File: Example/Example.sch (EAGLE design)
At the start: 26 parts, among them IC2 74LS02D, U1 CD4017

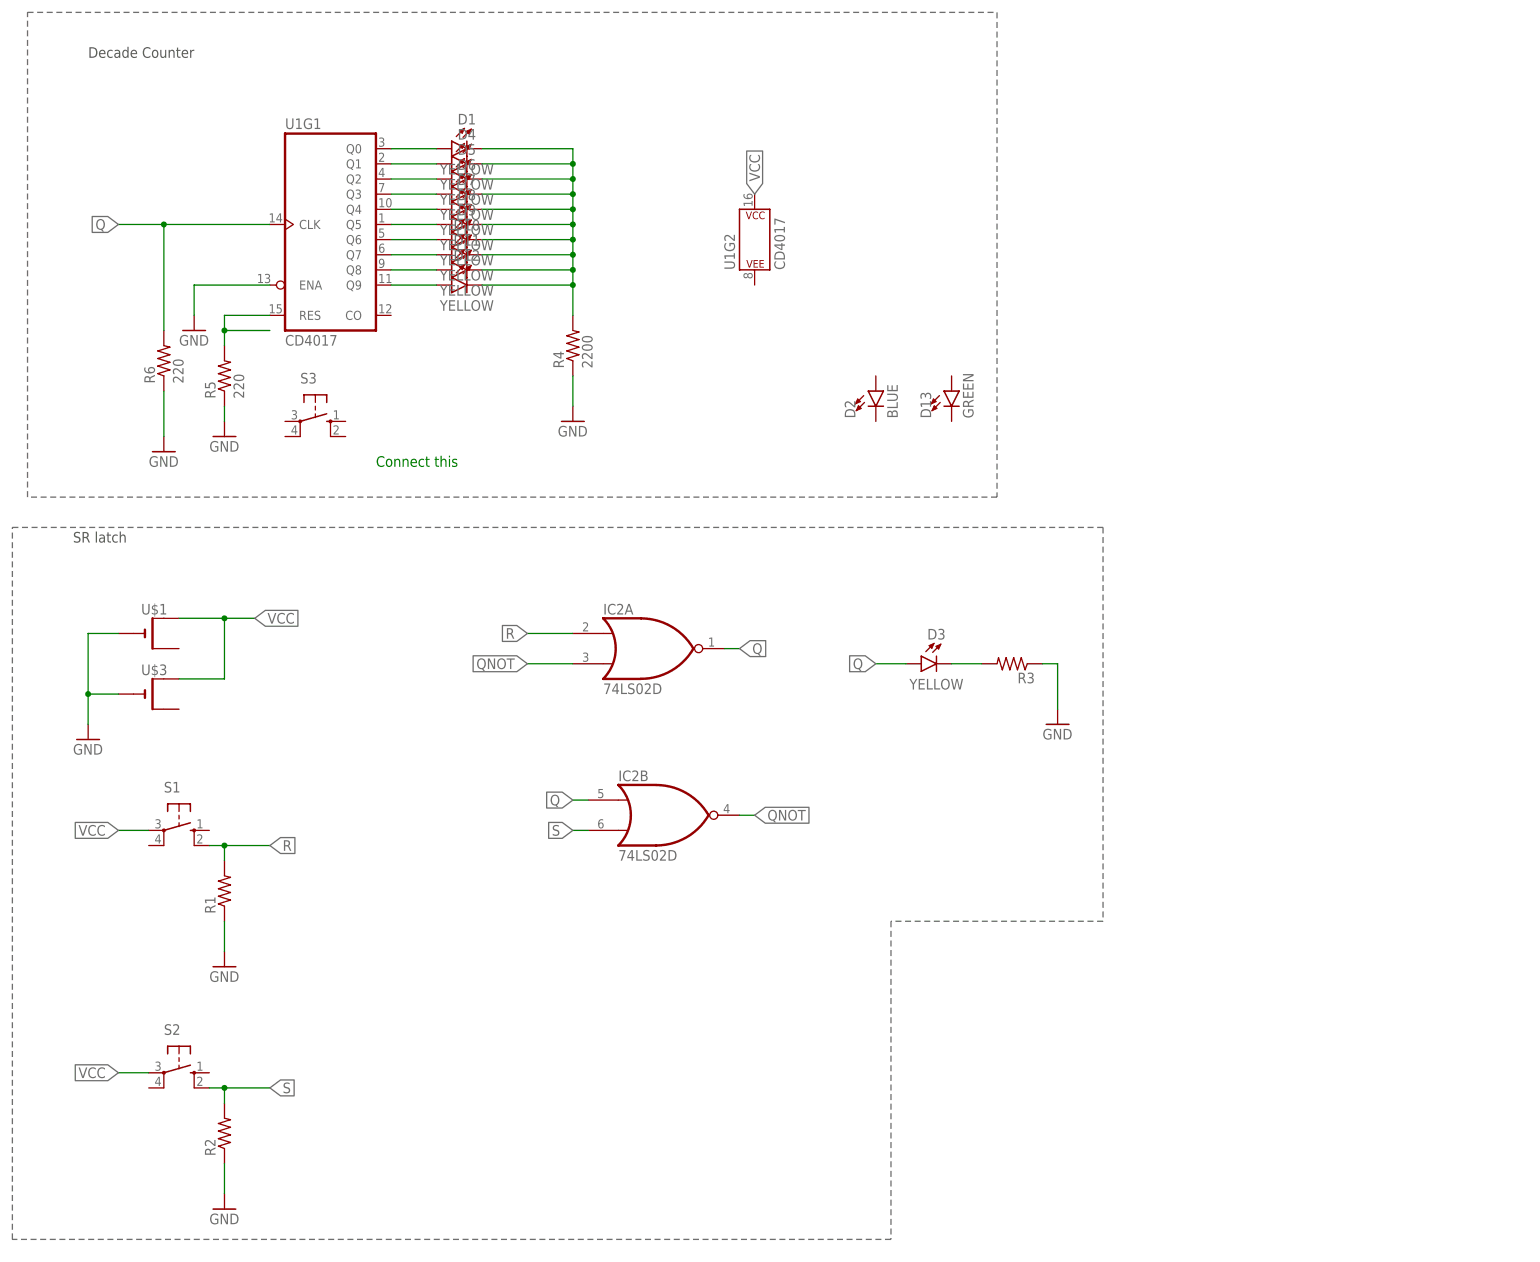
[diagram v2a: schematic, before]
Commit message: connected the reset button and change the titles for sheet
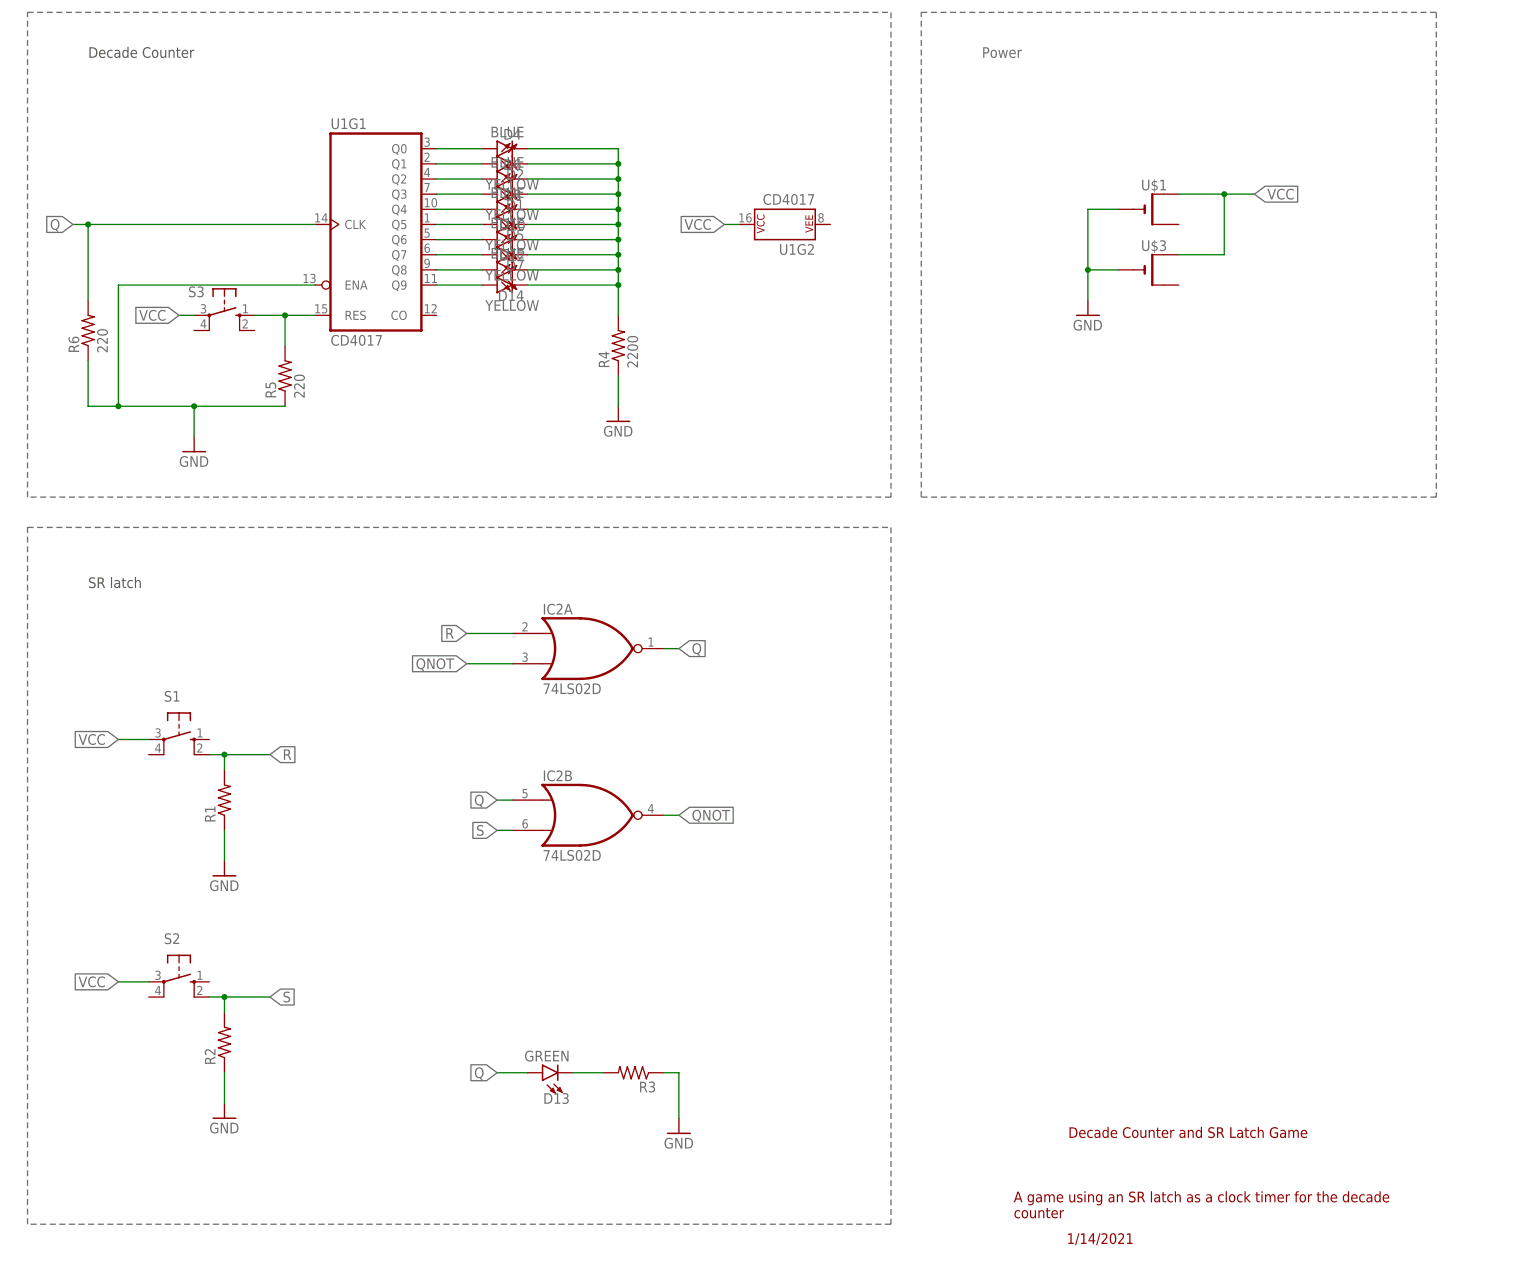
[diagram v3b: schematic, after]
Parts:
- removed D11, D3, D9: YELLOW, RoboJackets-LEDs:LED-SMD-YELLOW
- added D14: BLUE, RoboJackets-LEDs:LED-BLUE0603
- D1, D5, D7: value YELLOW -> BLUE; device RoboJackets-LEDs:LED-SMD-YELLOW -> RoboJackets-LEDs:LED-BLUE0603
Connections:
- removed net N$21: R5.2, U1G1.RES
- new net N$1: S3.P
- new net N$3: R5.2, S3.S, U1G1.RES
- net N$10: now also D2.A; no longer D1.A
- net N$12: now also D1.A; no longer D5.A
- net N$14: now also D5.A; no longer D7.A
- net N$16: now also D7.A; no longer D9.A
- net N$18: now also D14.A; no longer D11.A
- net N$2: now also D13.A; no longer D3.A
- net N$20: now also D14.C, D2.C; no longer D11.C, D9.C
- net N$5: now also D13.C; no longer D3.C
- net VCC: now also U1G2.P$V+
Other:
- note added: "1/14/2021"
- note added: "A game using an SR latch as a clock timer for the decade counter"
- note added: "Decade Counter and SR Latch Game"
- note added: "Power"
- note removed: "Connect this"
- moved on the sheet: D10, D12, D13, D2, D4, D6, D8, IC2A, IC2B, R1, R2, R3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

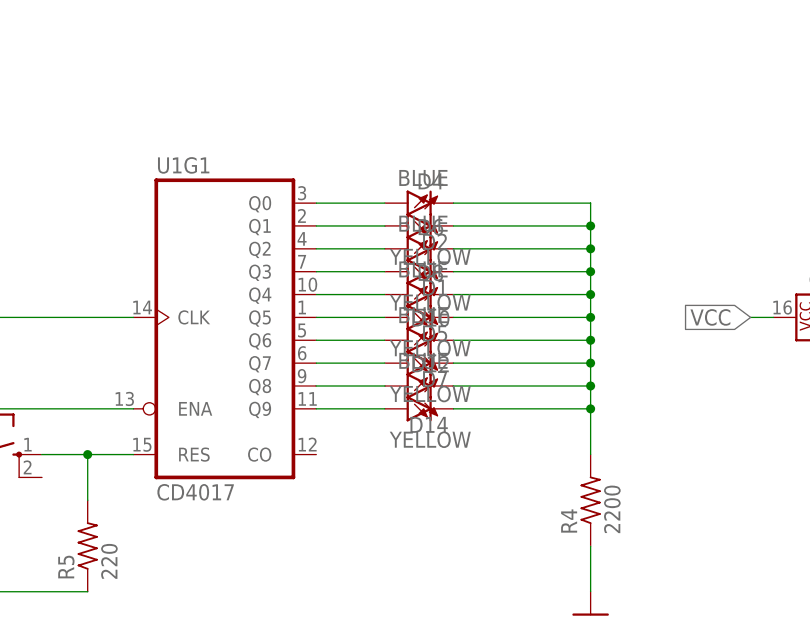
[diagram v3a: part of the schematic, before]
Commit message: change button and led position
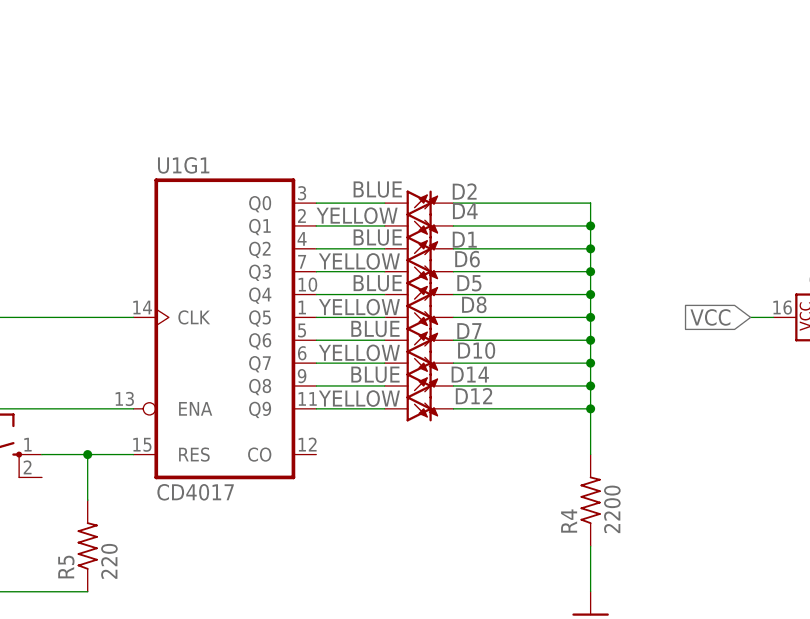
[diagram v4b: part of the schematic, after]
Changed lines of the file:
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@@
 </instance>
 <instance part="D4" gate="A" x="91.44" y="182.88" smashed="yes">
-<attribute name="NAME" x="91.44" y="186.944" size="1.778" layer="95" rot="MR0" align="bottom-center"/>
-<attribute name="VALUE" x="91.44" y="180.34" size="1.778" layer="96" rot="MR0" align="top-center"/>
+<attribute name="NAME" x="95.25" y="183.642" size="1.778" layer="95" rot="MR0" align="bottom-center"/>
+<attribute name="VALUE" x="83.312" y="184.912" size="1.778" layer="96" rot="MR0" align="top-center"/>
 </instance>
 <instance part="D6" gate="A" x="91.44" y="177.8" smashed="yes">
-<attribute name="NAME" x="91.44" y="181.864" size="1.778" layer="95" rot="MR0" align="bottom-center"/>
-<attribute name="VALUE" x="91.44" y="175.26" size="1.778" layer="96" rot="MR0" align="top-center"/>
+<attribute name="NAME" x="95.504" y="178.308" size="1.778" layer="95" rot="MR0" align="bottom-center"/>
+<attribute name="VALUE" x="83.566" y="179.832" size="1.778" layer="96" rot="MR0" align="top-center"/>
 </instance>
 <instance part="D8" gate="A" x="91.44" y="172.72" smashed="yes">
-<attribute name="NAME" x="91.44" y="176.784" size="1.778" layer="95" rot="MR0" align="bottom-center"/>
-<attribute name="VALUE" x="91.44" y="170.18" size="1.778" layer="96" rot="MR0" align="top-center"/>
+<attribute name="NAME" x="96.266" y="173.228" size="1.778" layer="95" rot="MR0" align="bottom-center"/>
+<attribute name="VALUE" x="83.566" y="174.752" size="1.778" layer="96" rot="MR0" align="top-center"/>
 </instance>
 <instance part="D10" gate="A" x="91.44" y="167.64" smashed="yes">
-<attribute name="NAME" x="91.44" y="171.704" size="1.778" layer="95" rot="MR0" align="bottom-center"/>
-<attribute name="VALUE" x="91.44" y="165.1" size="1.778" layer="96" rot="MR0" align="top-center"/>
+<attribute name="NAME" x="96.52" y="168.148" size="1.778" layer="95" rot="MR0" align="bottom-center"/>
+<attribute name="VALUE" x="83.566" y="169.672" size="1.778" layer="96" rot="MR0" align="top-center"/>
 </instance>
 <instance part="D12" gate="A" x="91.44" y="162.56" smashed="yes">
-<attribute name="NAME" x="91.44" y="166.624" size="1.778" layer="95" rot="MR0" align="bottom-center"/>
-<attribute name="VALUE" x="91.44" y="160.02" size="1.778" layer="96" rot="MR0" align="top-center"/>
+<attribute name="NAME" x="96.266" y="163.068" size="1.778" layer="95" rot="MR0" align="bottom-center"/>
+<attribute name="VALUE" x="83.566" y="164.592" size="1.778" layer="96" rot="MR0" align="top-center"/>
 </instance>
 <instance part="R4" gate="G$1" x="109.22" y="152.4" smashed="yes" rot="R90">
@@
 </instance>
 <instance part="D2" gate="G$1" x="88.9" y="185.42" smashed="yes" rot="R90">
-<attribute name="NAME" x="93.472" y="181.991" size="1.778" layer="95" font="vector" rot="R180"/>
-<attribute name="VALUE" x="93.472" y="187.325" size="1.778" layer="96" font="vector" rot="R180" align="top-left"/>
+<attribute name="NAME" x="96.774" y="187.579" size="1.778" layer="95" font="vector" rot="R180"/>
+<attribute name="VALUE" x="88.392" y="186.055" size="1.778" layer="96" font="vector" rot="R180" align="top-left"/>
 </instance>
 <instance part="D13" gate="G$1" x="96.52" y="30.48" smashed="yes" rot="R90">
@@
 </instance>
 <instance part="D14" gate="G$1" x="88.9" y="165.1" smashed="yes" rot="R90">
-<attribute name="NAME" x="93.472" y="161.671" size="1.778" layer="95" font="vector" rot="R180"/>
-<attribute name="VALUE" x="93.472" y="167.005" size="1.778" layer="96" font="vector" rot="R180" align="top-left"/>
+<attribute name="NAME" x="98.044" y="167.259" size="1.778" layer="95" font="vector" rot="R180"/>
+<attribute name="VALUE" x="88.138" y="165.481" size="1.778" layer="96" font="vector" rot="R180" align="top-left"/>
 </instance>
 <instance part="D1" gate="G$1" x="88.9" y="180.34" smashed="yes" rot="R90">
-<attribute name="NAME" x="93.472" y="176.911" size="1.778" layer="95" font="vector" rot="R180"/>
-<attribute name="VALUE" x="93.472" y="182.245" size="1.778" layer="96" font="vector" rot="R180" align="top-left"/>
+<attribute name="NAME" x="96.774" y="182.245" size="1.778" layer="95" font="vector" rot="R180"/>
+<attribute name="VALUE" x="88.392" y="180.721" size="1.778" layer="96" font="vector" rot="R180" align="top-left"/>
 </instance>
 <instance part="D5" gate="G$1" x="88.9" y="175.26" smashed="yes" rot="R90">
-<attribute name="NAME" x="93.472" y="171.831" size="1.778" layer="95" font="vector" rot="R180"/>
-<attribute name="VALUE" x="93.472" y="177.165" size="1.778" layer="96" font="vector" rot="R180" align="top-left"/>
+<attribute name="NAME" x="97.282" y="177.419" size="1.778" layer="95" font="vector" rot="R180"/>
+<attribute name="VALUE" x="88.392" y="175.641" size="1.778" layer="96" font="vector" rot="R180" align="top-left"/>
 </instance>
 <instance part="D7" gate="G$1" x="88.9" y="170.18" smashed="yes" rot="R90">
-<attribute name="NAME" x="93.472" y="166.751" size="1.778" layer="95" font="vector" rot="R180"/>
-<attribute name="VALUE" x="93.472" y="172.085" size="1.778" layer="96" font="vector" rot="R180" align="top-left"/>
+<attribute name="NAME" x="97.282" y="172.085" size="1.778" layer="95" font="vector" rot="R180"/>
+<attribute name="VALUE" x="88.138" y="170.561" size="1.778" layer="96" font="vector" rot="R180" align="top-left"/>
 </instance>
 </instances>

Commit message: small changes
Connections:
- net GND: now also IC2P.GND
- net VCC: now also IC2P.VCC
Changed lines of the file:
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@@
 <?xml version="1.0" encoding="utf-8"?>
 <!DOCTYPE eagle SYSTEM "eagle.dtd">
-<eagle version="9.5.2">
+<eagle version="9.5.1">
 <drawing>
 <settings>
@@
 <attribute name="VALUE" x="88.138" y="170.561" size="1.778" layer="96" font="vector" rot="R180" align="top-left"/>
 </instance>
+<instance part="IC2" gate="P" x="104.14" y="50.8" smashed="yes" rot="R90">
+<attribute name="NAME" x="107.315" y="55.245" size="1.778" layer="95" rot="R180"/>
+</instance>
 </instances>
 <busses>
@@
 <junction x="38.1" y="142.24"/>
 </segment>
+<segment>
+<pinref part="IC2" gate="P" pin="GND"/>
+<wire x1="114.3" y1="50.8" x2="116.84" y2="50.8" width="0.1524" layer="91"/>
+<label x="116.84" y="50.8" size="1.778" layer="95" xref="yes"/>
+</segment>
 </net>
 <net name="QNOT" class="0">
@@
 <pinref part="IC2" gate="B" pin="O"/>
 <wire x1="119.38" y1="73.66" x2="116.84" y2="73.66" width="0.1524" layer="91"/>
+</segment>
+<segment>
+<label x="88.9" y="30.48" size="1.778" layer="95" rot="R180" xref="yes"/>
 </segment>
 </net>
@@
 <wire x1="116.84" y1="101.6" x2="119.38" y2="101.6" width="0.1524" layer="91"/>
 <label x="119.38" y="101.6" size="1.778" layer="95" xref="yes"/>
-</segment>
-<segment>
-<label x="88.9" y="30.48" size="1.778" layer="95" rot="R180" xref="yes"/>
 </segment>
 <segment>
@@
 <label x="127" y="172.72" size="1.778" layer="95" rot="R180" xref="yes"/>
 </segment>
+<segment>
+<pinref part="IC2" gate="P" pin="VCC"/>
+<wire x1="93.98" y1="50.8" x2="91.44" y2="50.8" width="0.1524" layer="91"/>
+<label x="91.44" y="50.8" size="1.778" layer="95" rot="R180" xref="yes"/>
+</segment>
 </net>
